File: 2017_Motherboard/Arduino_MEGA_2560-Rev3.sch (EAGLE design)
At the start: 78 parts, among them IC1 NCP1117ST50T3G, IC2 FT232RL, IC3 ATMEGA2560-16AU, IC7 LMV358IDGKR, X1 POWERSUPPLY_DC21MMX, Y1 CSTCE16M0V53-R0 16MHZ

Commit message: SchematicRev1
finished the schematic (hopefully), now we will work on the layout
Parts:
- added D2: RED, SparkFun-LED:LED-RED0603
- added J10, J11: (no value), SparkFun-Connectors:M02PTH
- added J12: (no value), SparkFun-Connectors:M06LONGPADS
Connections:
- new net N$15: D2.C, J11.2
- net +3V3: now also J10.1
- net +5V: now also J11.1, J12.2
- net FTDI_3.3V: now also J10.2
- net GND: now also J12.3
- net PA1: now also J12.6
- net PA2: now also J12.1
- net RXD1: now also J12.4
- net TXD1: now also J12.5
- net V_USB: now also D2.A
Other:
- note added: "ADC0-7"
- note added: "Bluetooth Connection"
- note added: "EN"
- note added: "GND"
- note added: "PA0"
- note added: "PA1"
- note added: "PA2"
- note added: "PE0"
- note added: "PE1"
- note added: "RXD"
- note added: "RXD1"
- note added: "State"
- note added: "TXD"
- note added: "TXD1"
- note added: "Used Pins:"
- note added: "VCC"
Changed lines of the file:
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@@
 <?xml version="1.0" encoding="utf-8"?>
 <!DOCTYPE eagle SYSTEM "eagle.dtd">
-<eagle version="7.6.0">
+<eagle version="7.7.0">
 <drawing>
 <settings>
@@
 <part name="J8" library="SparkFun-Connectors" deviceset="M02" device="PTH"/>
 <part name="J9" library="SparkFun-Connectors" deviceset="M06" device="LONGPADS"/>
+<part name="J10" library="SparkFun-Connectors" deviceset="M02" device="PTH"/>
+<part name="J11" library="SparkFun-Connectors" deviceset="M02" device="PTH"/>
+<part name="J12" library="SparkFun-Connectors" deviceset="M06" device="LONGPADS"/>
+<part name="D2" library="SparkFun-LED" deviceset="LED-RED" device="0603" value="RED"/>
 </parts>
 <sheets>
@@
 <text x="294.64" y="86.36" size="1.778" layer="91">PA0 can be used as an INT</text>
 <text x="269.24" y="124.46" size="1.778" layer="91">I2C address: 0x28</text>
+<text x="345.44" y="-63.5" size="1.778" layer="91">Bluetooth Connection</text>
+<text x="363.22" y="-86.36" size="1.778" layer="91">State</text>
+<text x="363.22" y="-88.9" size="1.778" layer="91">RXD</text>
+<text x="363.22" y="-91.44" size="1.778" layer="91">TXD</text>
+<text x="363.22" y="-93.98" size="1.778" layer="91">GND</text>
+<text x="363.22" y="-96.52" size="1.778" layer="91">VCC</text>
+<text x="363.22" y="-99.06" size="1.778" layer="91">EN</text>
+<text x="421.64" y="167.64" size="1.778" layer="91">Used Pins:</text>
+<text x="421.64" y="162.56" size="1.778" layer="91">PE0</text>
+<text x="421.64" y="160.02" size="1.778" layer="91">PE1</text>
+<text x="421.64" y="157.48" size="1.778" layer="91">TXD1</text>
+<text x="421.64" y="154.94" size="1.778" layer="91">RXD1</text>
+<text x="421.64" y="152.4" size="1.778" layer="91">PA0</text>
+<text x="421.64" y="149.86" size="1.778" layer="91">PA1</text>
+<text x="421.64" y="147.32" size="1.778" layer="91">PA2</text>
+<text x="421.64" y="144.78" size="1.778" layer="91">ADC0-7</text>
 </plain>
 <instances>
@@
 <instance part="Y1" gate="G$1" x="55.88" y="129.54" smashed="yes">
 <attribute name="NAME" x="50.8" y="134.112" size="1.778" layer="95"/>
-<attribute name="VALUE" x="45.72" y="121.412" size="1.778" layer="96"/>
+<attribute name="VALUE" x="58.42" y="129.032" size="1.778" layer="96"/>
 </instance>
 <instance part="GND20" gate="1" x="40.64" y="129.54" smashed="yes" rot="R270">
@@
 <instance part="J8" gate="G$1" x="337.82" y="127" rot="R180"/>
 <instance part="J9" gate="G$1" x="261.62" y="38.1" rot="MR0"/>
+<instance part="J10" gate="G$1" x="152.4" y="-76.2" rot="R180"/>
+<instance part="J11" gate="G$1" x="104.14" y="-48.26" rot="R180"/>
+<instance part="J12" gate="G$1" x="355.6" y="-93.98" rot="MR0"/>
+<instance part="D2" gate="G$1" x="93.98" y="-60.96" rot="R180"/>
 </instances>
 <busses>
@@
 <pinref part="P+12" gate="1" pin="+5V"/>
 </segment>
+<segment>
+<pinref part="J11" gate="G$1" pin="1"/>
+<wire x1="96.52" y1="-48.26" x2="86.36" y2="-48.26" width="0.1524" layer="91"/>
+<label x="88.9" y="-48.26" size="1.778" layer="95"/>
+</segment>
+<segment>
+<pinref part="J12" gate="G$1" pin="2"/>
+<wire x1="350.52" y1="-96.52" x2="335.28" y2="-96.52" width="0.1524" layer="91"/>
+<label x="340.36" y="-96.52" size="1.778" layer="95"/>
+</segment>
 </net>
 <net name="GND" class="2">
@@
 <label x="254" y="25.4" size="1.778" layer="95" rot="R90"/>
 </segment>
+<segment>
+<pinref part="J12" gate="G$1" pin="3"/>
+<wire x1="350.52" y1="-93.98" x2="335.28" y2="-93.98" width="0.1524" layer="91"/>
+<label x="340.36" y="-93.98" size="1.778" layer="95"/>
+</segment>
 </net>
 <net name="AREF" class="0">
@@
 <label x="322.58" y="129.54" size="1.778" layer="95" rot="R180"/>
 </segment>
+<segment>
+<pinref part="J10" gate="G$1" pin="1"/>
+<wire x1="144.78" y1="-76.2" x2="132.08" y2="-76.2" width="0.1524" layer="91"/>
+<label x="134.62" y="-76.2" size="1.778" layer="95"/>
+</segment>
 </net>
 <net name="SDA" class="0">
@@
 <pinref part="COMMUNICATION" gate="A" pin="3"/>
 </segment>
+<segment>
+<pinref part="J12" gate="G$1" pin="4"/>
+<wire x1="350.52" y1="-91.44" x2="335.28" y2="-91.44" width="0.1524" layer="91"/>
+<label x="340.36" y="-91.44" size="1.778" layer="95"/>
+</segment>
 </net>
 <net name="TXD1" class="0">
@@
 <pinref part="COMMUNICATION" gate="A" pin="4"/>
 </segment>
+<segment>
+<pinref part="J12" gate="G$1" pin="5"/>
+<wire x1="350.52" y1="-88.9" x2="335.28" y2="-88.9" width="0.1524" layer="91"/>
+<label x="340.36" y="-88.9" size="1.778" layer="95"/>
+</segment>
 </net>
 <net name="RXD2" class="0">
@@
 <pinref part="XIO" gate="A" pin="4"/>
 </segment>
+<segment>
+<pinref part="J12" gate="G$1" pin="6"/>
+<wire x1="350.52" y1="-86.36" x2="335.28" y2="-86.36" width="0.1524" layer="91"/>
+<label x="340.36" y="-86.36" size="1.778" layer="95"/>
+</segment>
 </net>
 <net name="PA2" class="0">
@@
 <label x="32.385" y="51.435" size="1.778" layer="95"/>
 <pinref part="XIO" gate="A" pin="5"/>
+</segment>
+<segment>
+<pinref part="J12" gate="G$1" pin="1"/>
+<wire x1="350.52" y1="-99.06" x2="335.28" y2="-99.06" width="0.1524" layer="91"/>
+<label x="340.36" y="-99.06" size="1.778" layer="95"/>
 </segment>
 </net>
@@
 <segment>
 <pinref part="IC2" gate="1" pin="3V3OUT"/>
-<wire x1="175.26" y1="-88.9" x2="134.62" y2="-88.9" width="0.1524" layer="91"/>
+<wire x1="175.26" y1="-88.9" x2="142.24" y2="-88.9" width="0.1524" layer="91"/>
 <pinref part="C17" gate="G$1" pin="1"/>
 <label x="154.94" y="-88.9" size="1.778" layer="95"/>
+<pinref part="J10" gate="G$1" pin="2"/>
+<wire x1="142.24" y1="-88.9" x2="134.62" y2="-88.9" width="0.1524" layer="91"/>
+<wire x1="144.78" y1="-78.74" x2="142.24" y2="-78.74" width="0.1524" layer="91"/>
+<wire x1="142.24" y1="-78.74" x2="142.24" y2="-88.9" width="0.1524" layer="91"/>
+<junction x="142.24" y="-88.9"/>
 </segment>
 <segment>
@@
 <segment>
 <pinref part="J5" gate="G$1" pin="VBUS"/>
-<wire x1="78.74" y1="-68.58" x2="101.6" y2="-68.58" width="0.1524" layer="91"/>
+<wire x1="78.74" y1="-68.58" x2="93.98" y2="-68.58" width="0.1524" layer="91"/>
 <pinref part="SUPPLY3" gate="G$1" pin="V_USB"/>
+<wire x1="93.98" y1="-68.58" x2="101.6" y2="-68.58" width="0.1524" layer="91"/>
 <wire x1="101.6" y1="-68.58" x2="114.3" y2="-68.58" width="0.1524" layer="91"/>
 <wire x1="114.3" y1="-68.58" x2="119.38" y2="-68.58" width="0.1524" layer="91"/>
@@
 <wire x1="114.3" y1="-68.58" x2="114.3" y2="-73.66" width="0.1524" layer="91"/>
 <junction x="114.3" y="-68.58"/>
+<pinref part="D2" gate="G$1" pin="A"/>
+<wire x1="93.98" y1="-63.5" x2="93.98" y2="-68.58" width="0.1524" layer="91"/>
+<junction x="93.98" y="-68.58"/>
 </segment>
 </net>
@@
 </segment>
 </net>
+<net name="N$15" class="0">
+<segment>
+<pinref part="J11" gate="G$1" pin="2"/>
+<pinref part="D2" gate="G$1" pin="C"/>
+<wire x1="96.52" y1="-50.8" x2="93.98" y2="-50.8" width="0.1524" layer="91"/>
+<wire x1="93.98" y1="-50.8" x2="93.98" y2="-55.88" width="0.1524" layer="91"/>
+</segment>
+</net>

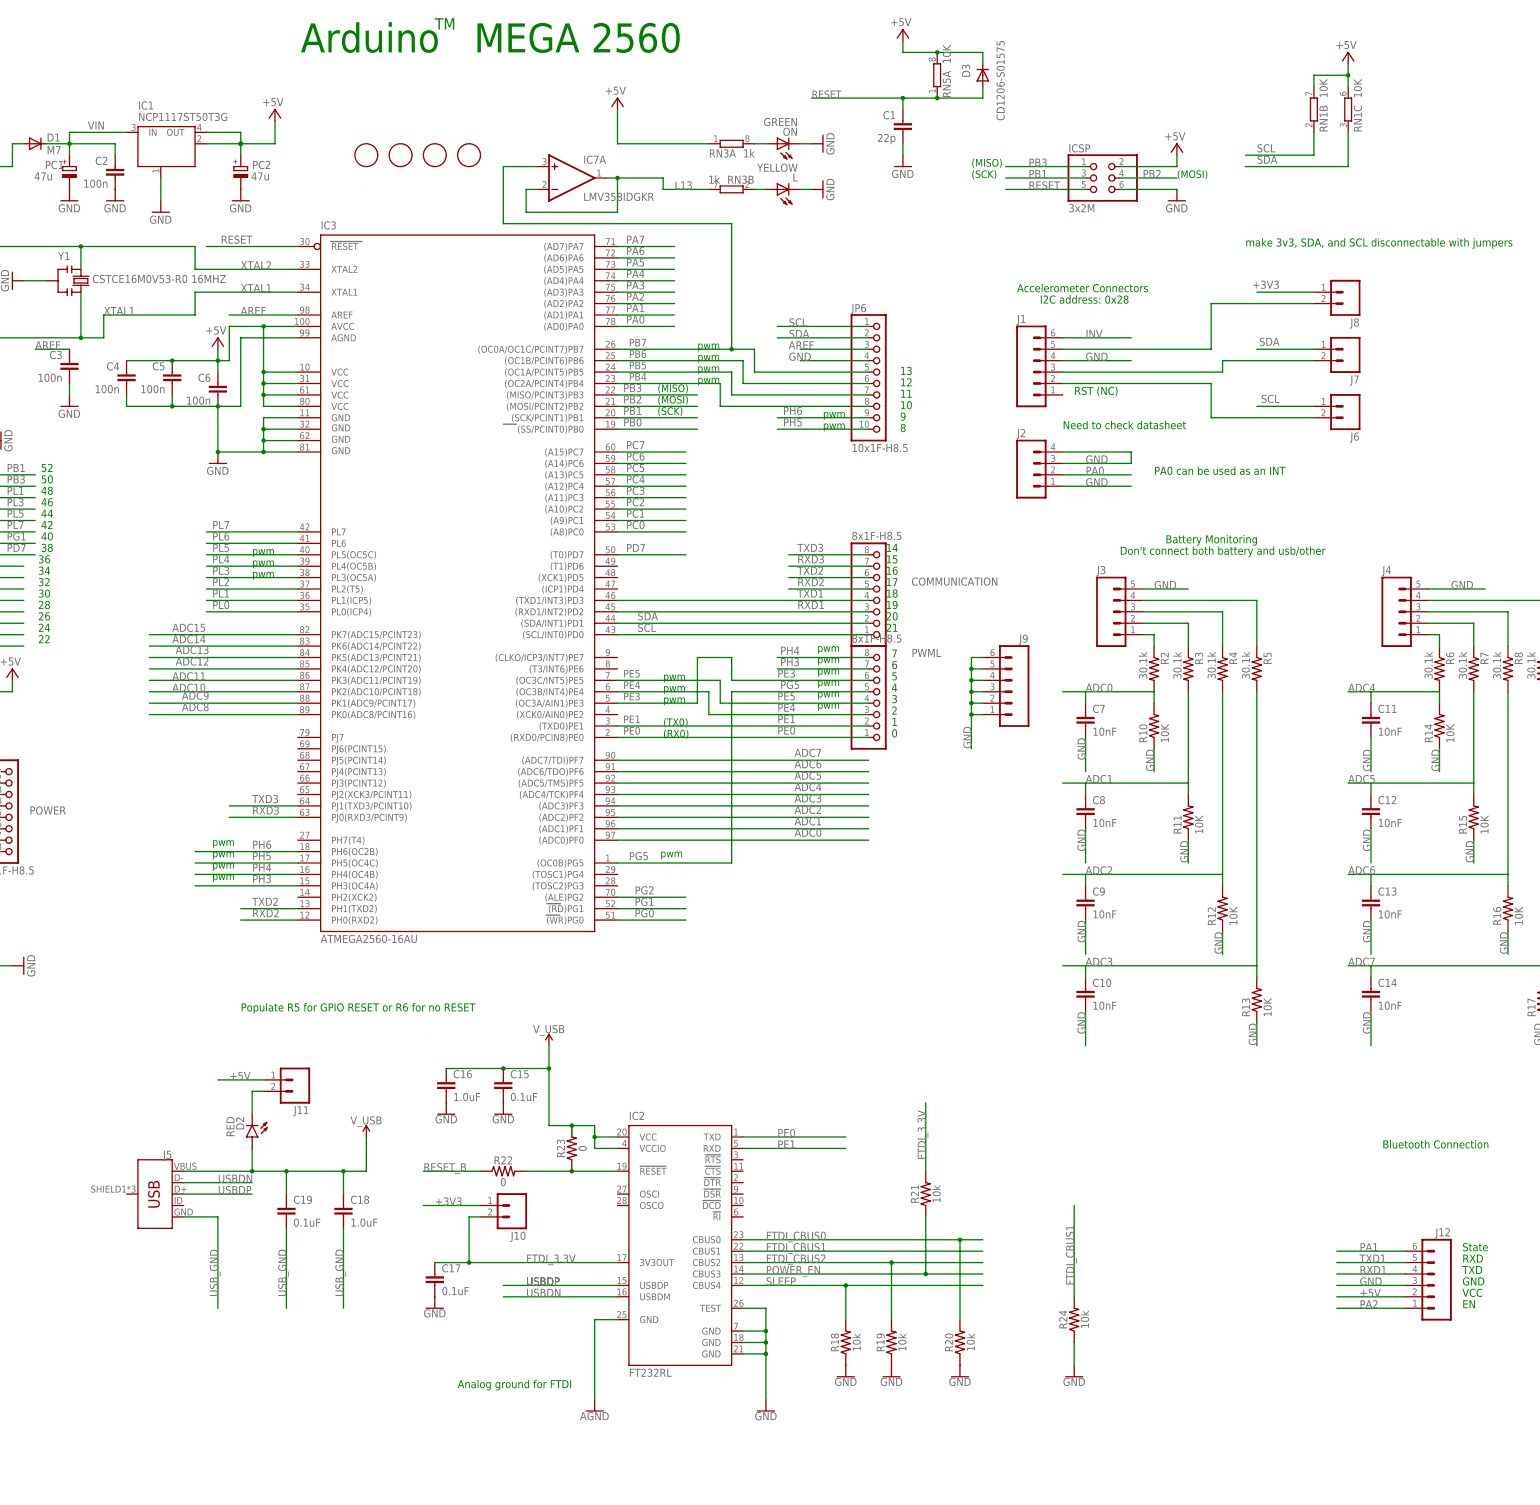
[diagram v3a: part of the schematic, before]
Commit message: switched led on USB line to parallel
LED will now not drop the voltage
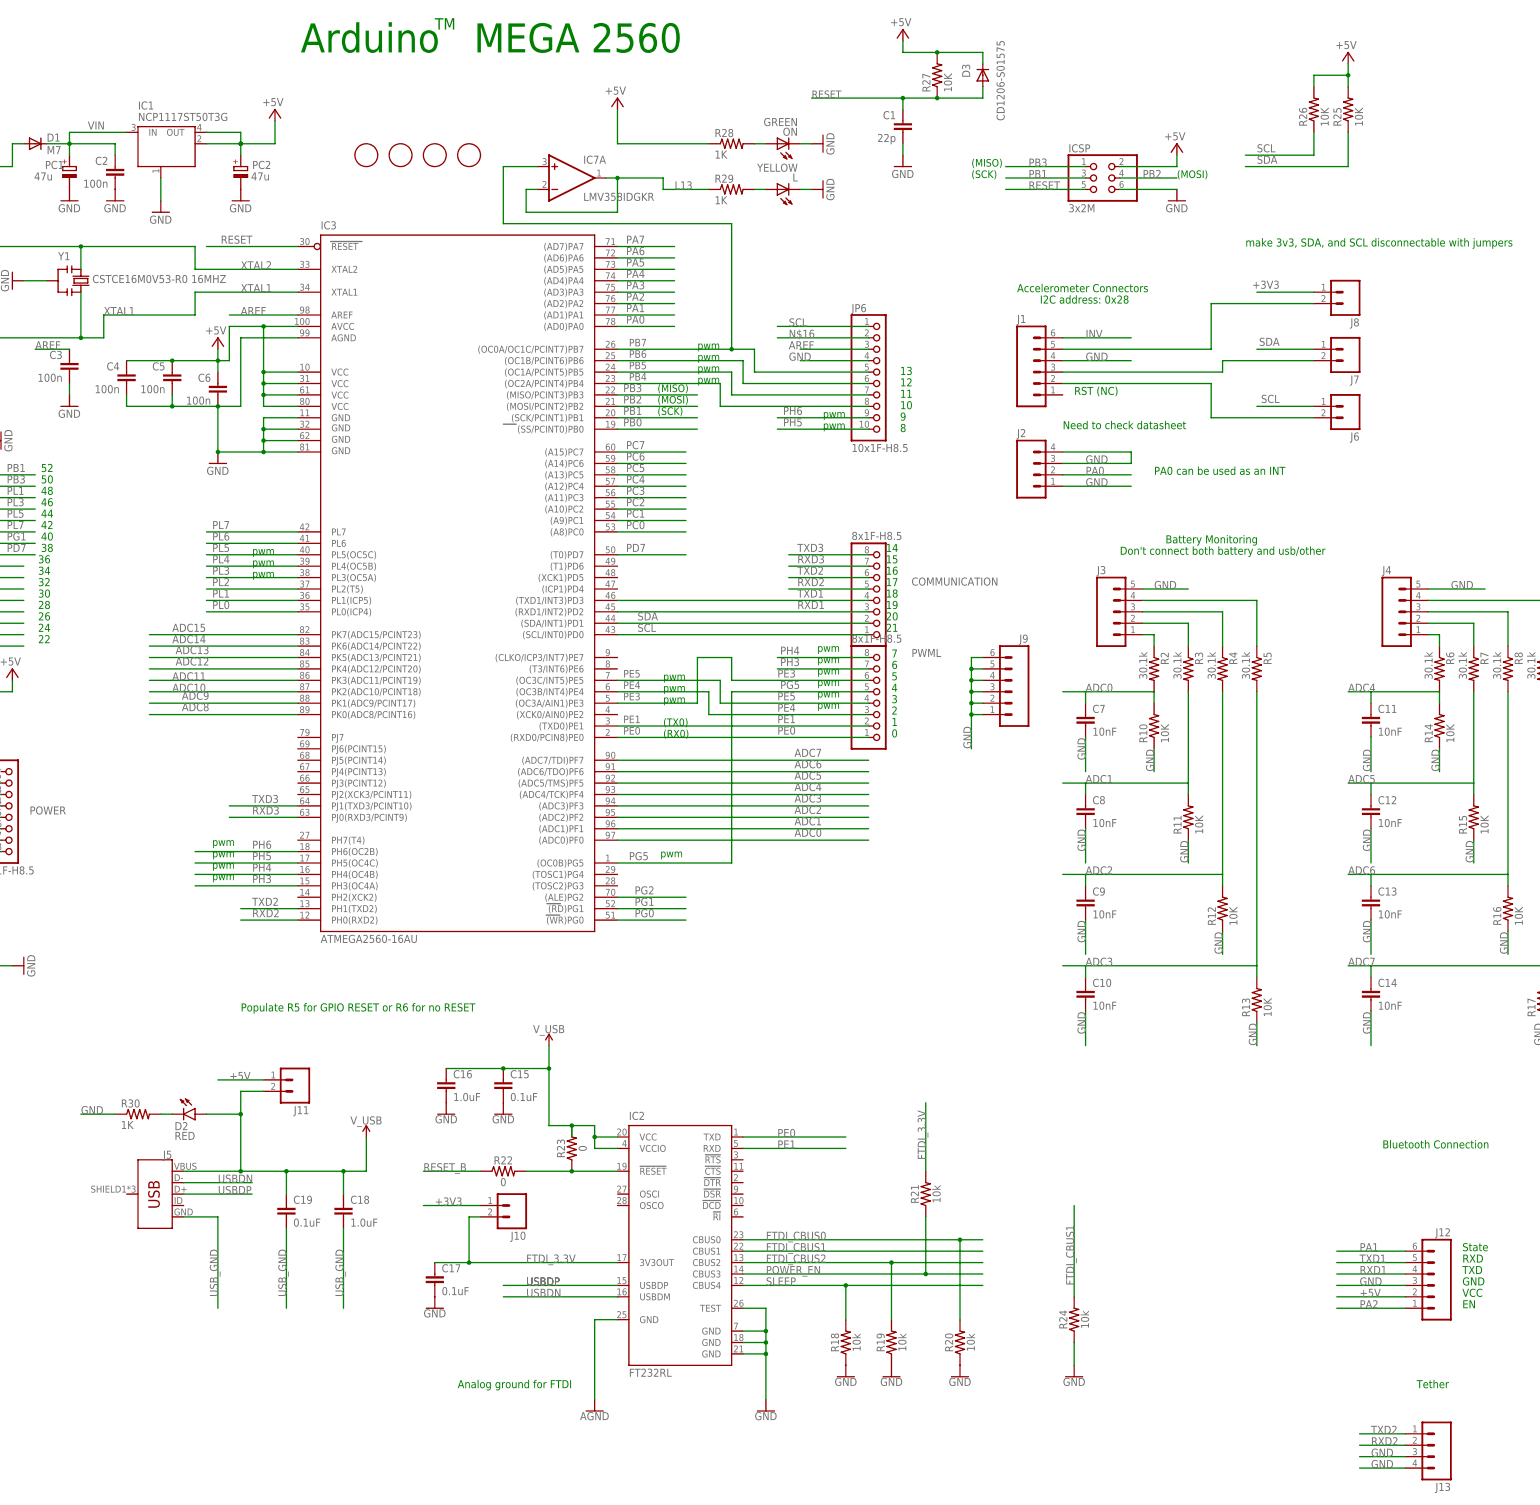
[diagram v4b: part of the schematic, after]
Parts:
- removed RN1, RN5: 10K, resistor-dil:4R-NCAT16
- removed RN3: 1k, resistor-dil:4R-NCAY16
- added J13: (no value), SparkFun-Connectors:M04LONGPADS
- added R25, R26, R27: 10K, SparkFun-Resistors:10KOHM-1/10W-1%(0603)0603
- added R28, R29, R30: 1K, SparkFun-Resistors:1KOHM-1/10W-1%(0603)
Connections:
- new net N$16: JP6.2
- net +5V: now also R25.2, R26.2, R27.2, R28.1; no longer RN1B.2, RN1C.2, RN3A.1, RN5A.2
- net GND: now also J13.3, J13.4, R30.1
- net L13: now also R29.1; no longer RN3B.2
- net N$15: now also R30.2; no longer J11.2
- net N$2: now also R29.2; no longer RN3B.1
- net N$3: now also R28.2; no longer RN3A.2
- net RESET: now also R27.1; no longer RN5A.1
- net RXD2: now also J13.2
- net SCL: now also R26.1; no longer RN1B.1
- net SDA: now also R25.1; no longer JP6.2, RN1C.1
- net TXD2: now also J13.1
- net V_USB: now also J11.2
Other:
- note added: "Tether"
- moved on the sheet: D2

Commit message: Reverted schematic and Layout
took out video and and added support for orientation sensor. schematic
and layout are in sync again
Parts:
- removed XIO: 18x2F-H8.5, SmartPrj:PINHD-2X18
- added BLUETOOTH_J6, ESC_PWM_GND: (no value), SparkFun-Connectors:M06LONGPADS
- added IC4: MAX4312ESE, maxim:MAX4312ESE
- added IC5: MAX3468CPA, maxim:MAX3468CPA
- added RXD2_JUMPER, TXD2_JUMPER: (no value), SparkFun-Connectors:M02PTH
- added VIDEO_IN, VIDEO_IN_GND: 8x1F-H8.5, SmartPrj:PINHD-1X8
- added VIDEO_OUT: A1944-50, con-coax:A1944-50
- J12, J9: device SparkFun-Connectors:M06LONGPADS -> SparkFun-Connectors:M13
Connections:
- removed net INV: J1.6
- removed net RESET_B: R22.1
- new net RXD2_OUT: IC5.A, J13.2, RXD2_JUMPER.2
- new net TXD2_OUT: IC5.B, J13.1, TXD2_JUMPER.2
- new net VIDEO_OUT: IC4.OUT, VIDEO_OUT.1
- new net VID_0: IC4.IN0, VIDEO_IN.1
- new net VID_1: IC4.IN1, VIDEO_IN.2
- new net VID_2: IC4.IN2, VIDEO_IN.3
- new net VID_3: IC4.IN3, VIDEO_IN.4
- new net VID_4: IC4.IN4, VIDEO_IN.5
- new net VID_5: IC4.IN5, VIDEO_IN.6
- new net VID_6: IC4.IN6, VIDEO_IN.7
- new net VID_7: IC4.IN7, VIDEO_IN.8
- net +5V: now also BLUETOOTH_J6.2, IC4.V+, IC5.VCC, J1.6, J12.13; no longer J12.2, XIO.1, XIO.2
- net GND: now also BLUETOOTH_J6.3, ESC_PWM_GND.1, ESC_PWM_GND.2, ESC_PWM_GND.3, ESC_PWM_GND.4, ESC_PWM_GND.5, ESC_PWM_GND.6, IC4.!SHDN, IC4.FB, IC4.V-, IC5.GND, VIDEO_IN_GND.1, VIDEO_IN_GND.2, VIDEO_IN_GND.3, VIDEO_IN_GND.4, VIDEO_IN_GND.5, VIDEO_IN_GND.6, VIDEO_IN_GND.7, VIDEO_IN_GND.8, VIDEO_OUT.2; no longer J12.3, J9.2, J9.3, J9.4, J9.5, J9.6, XIO.35, XIO.36
- net PA0: no longer XIO.3
- net PA1: now also BLUETOOTH_J6.6; no longer J12.6, XIO.4
- net PA2: now also BLUETOOTH_J6.1; no longer J12.1, XIO.5
- net PA3: now also IC4.A0; no longer XIO.6
- net PA4: now also IC4.A1; no longer XIO.7
- net PA5: now also IC4.A2; no longer XIO.8
- net PA6: now also IC5.RE/; no longer XIO.9
- net PA7: now also IC5.DE; no longer XIO.10
- net PB0: now also J12.1; no longer XIO.34
- net PB1: now also J9.13; no longer XIO.33
- net PB2: now also J12.2; no longer XIO.32
- net PB3: now also J9.12; no longer XIO.31
- net PC0: now also J12.9; no longer XIO.18
- net PC1: now also J9.5; no longer XIO.17
- net PC2: now also J12.10; no longer XIO.16
- net PC3: now also J9.4; no longer XIO.15
- net PC4: now also J12.11; no longer XIO.14
- net PC5: now also J9.3; no longer XIO.13
- net PC6: now also J12.12; no longer XIO.12
- net PC7: now also J9.2; no longer XIO.11
- net PD7: now also J9.6; no longer XIO.19
- net PG0: now also J12.7; no longer XIO.22
- net PG1: now also J9.7; no longer XIO.21
- net PG2: now also J12.8; no longer XIO.20
- net PL0: now also J12.3; no longer XIO.30
- net PL1: now also J9.11; no longer XIO.29
- net PL2: now also J12.4; no longer XIO.28
- net PL3: now also J9.10; no longer XIO.27
- net PL4: now also J12.5; no longer XIO.26
- net PL5: now also J9.9; no longer XIO.25
- net PL6: now also J12.6; no longer XIO.24
- net PL7: now also J9.8; no longer XIO.23
- net RESET: now also R22.1
- net RXD1: now also BLUETOOTH_J6.4; no longer J12.4
- net RXD2: now also IC5.RO, RXD2_JUMPER.1; no longer J13.2
- net TXD1: now also BLUETOOTH_J6.5; no longer J12.5
- net TXD2: now also IC5.DI, TXD2_JUMPER.1; no longer J13.1
- net V_USB: now also R23.2
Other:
- note added: "Close these jumpers if no RS485 transciever used"
- note added: "Output Transciever"
- note added: "PC0"
- note added: "PC1"
- note added: "PC2"
- note added: "Video Switching"
- note added: "changed RESET_B to RESET"
- note removed: "22"
- note removed: "23"
- note removed: "24"
- note removed: "25"
- note removed: "26"
- note removed: "27"
- note removed: "28"
- note removed: "29"
- moved on the sheet: J13
